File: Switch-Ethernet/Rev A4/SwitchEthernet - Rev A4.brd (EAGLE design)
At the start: 86 x 90 mm, 110 parts, among them J1 22-05-7028-02, J2 DF17(2.0)-20DP-0.5V(57), J3 DF17(4.0)-20DP-0.5V(57), J4 22-05-7058-05, P1 RB1-125BAG1A, T1 H1102FNL, T2 H1102FNL, U1 TC1264-3.3, U2 TC1264-1.8, U3 KSZ8995MA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

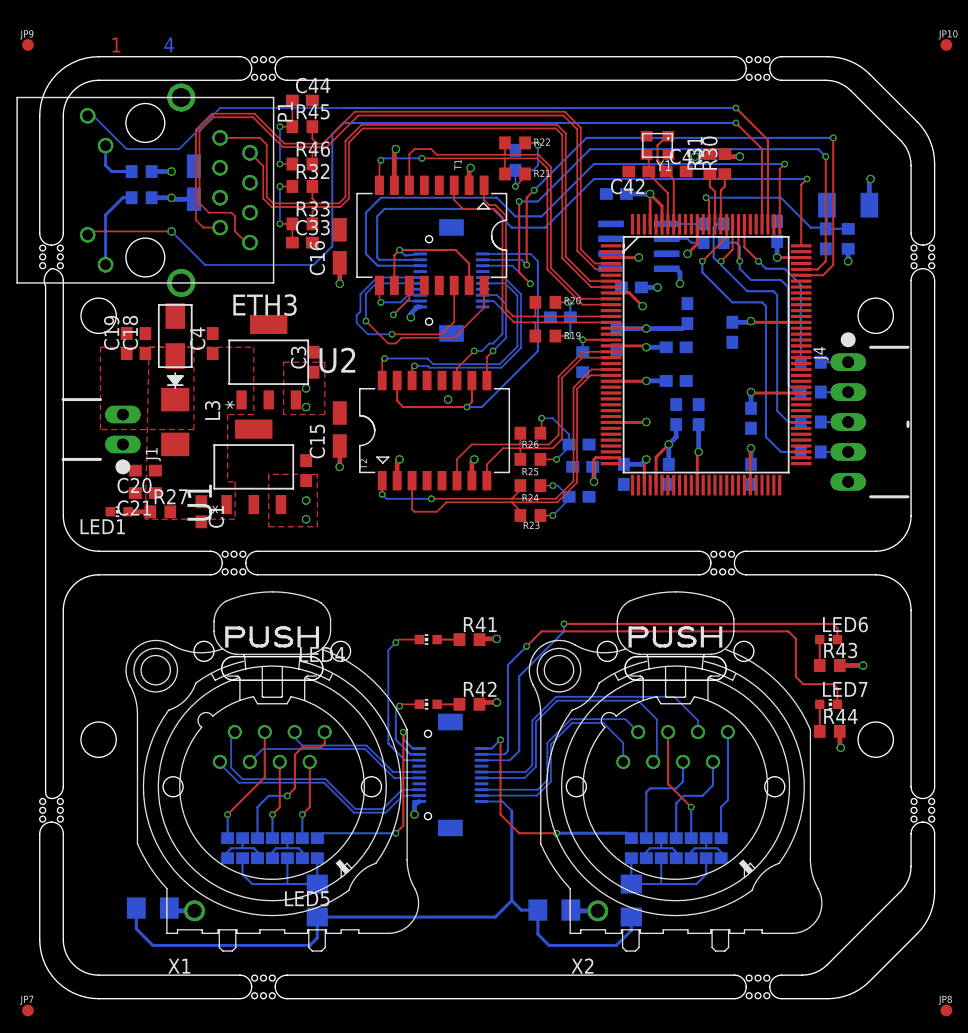
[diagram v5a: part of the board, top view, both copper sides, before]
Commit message: Add via to the guard ring
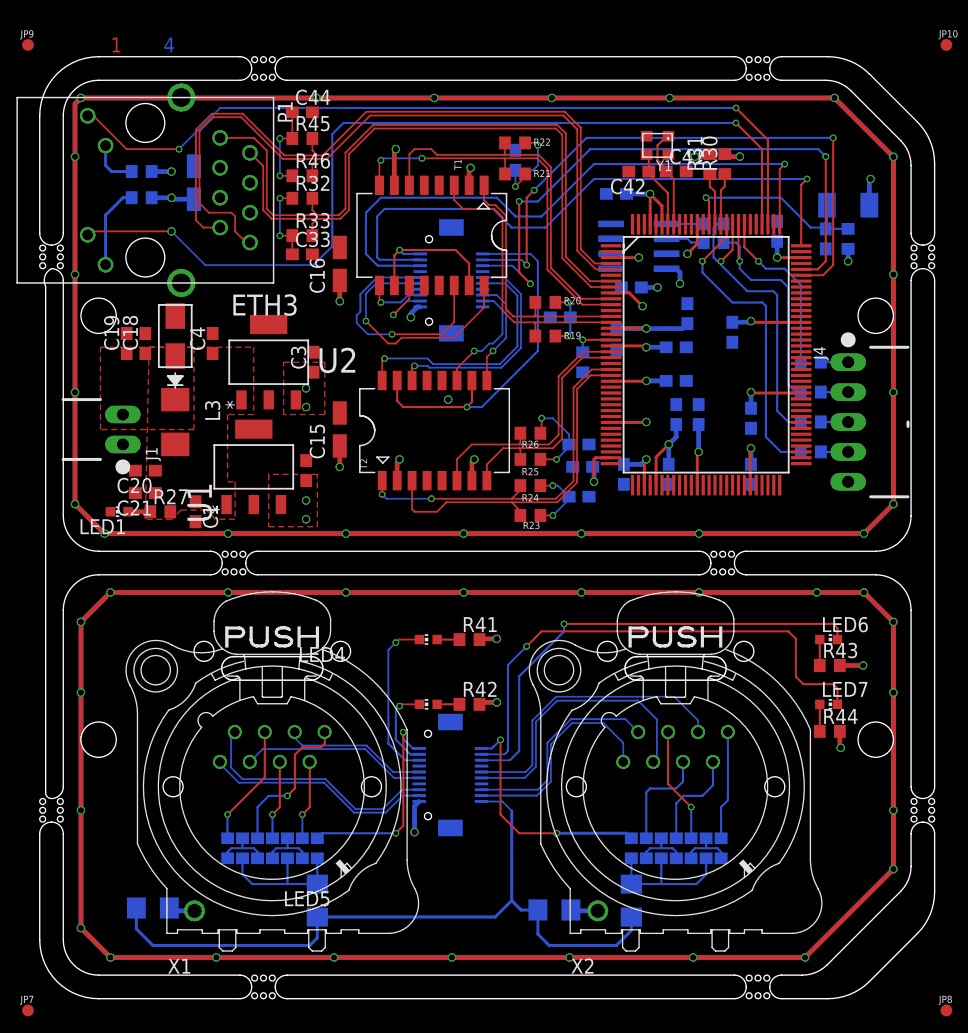
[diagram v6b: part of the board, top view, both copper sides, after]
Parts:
- moved C16 1.50 mm to (30.5, 67.4)
- moved C33 1.00 mm to (27.3, 68.2)
- moved C44 1.00 mm to (27.3, 80.3)
- moved R32 1.00 mm to (27.3, 73.0)
- moved R33 1.00 mm to (27.3, 69.8)
- moved R45 1.00 mm to (27.3, 78.1)
- moved R46 1.00 mm to (27.3, 74.9)
- moved C1 0.50 mm to (18.2, 46.4)
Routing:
- net N$2: track 0.00 -> 413.7 mm, vias 0 -> 21
- net N$1: track 0.00 -> 382.4 mm, vias 0 -> 23
- net +3V3: track 67.0 -> 68.4 mm
- net TX3_ISO_N: track 53.1 -> 54.5 mm
- net TX3_ISO_P: track 56.9 -> 58.0 mm
- net RX3_ISO_P: track 61.0 -> 61.8 mm
- net RX3_ISO_N: track 63.2 -> 64.0 mm
- net L3-2: vias 1 -> 2

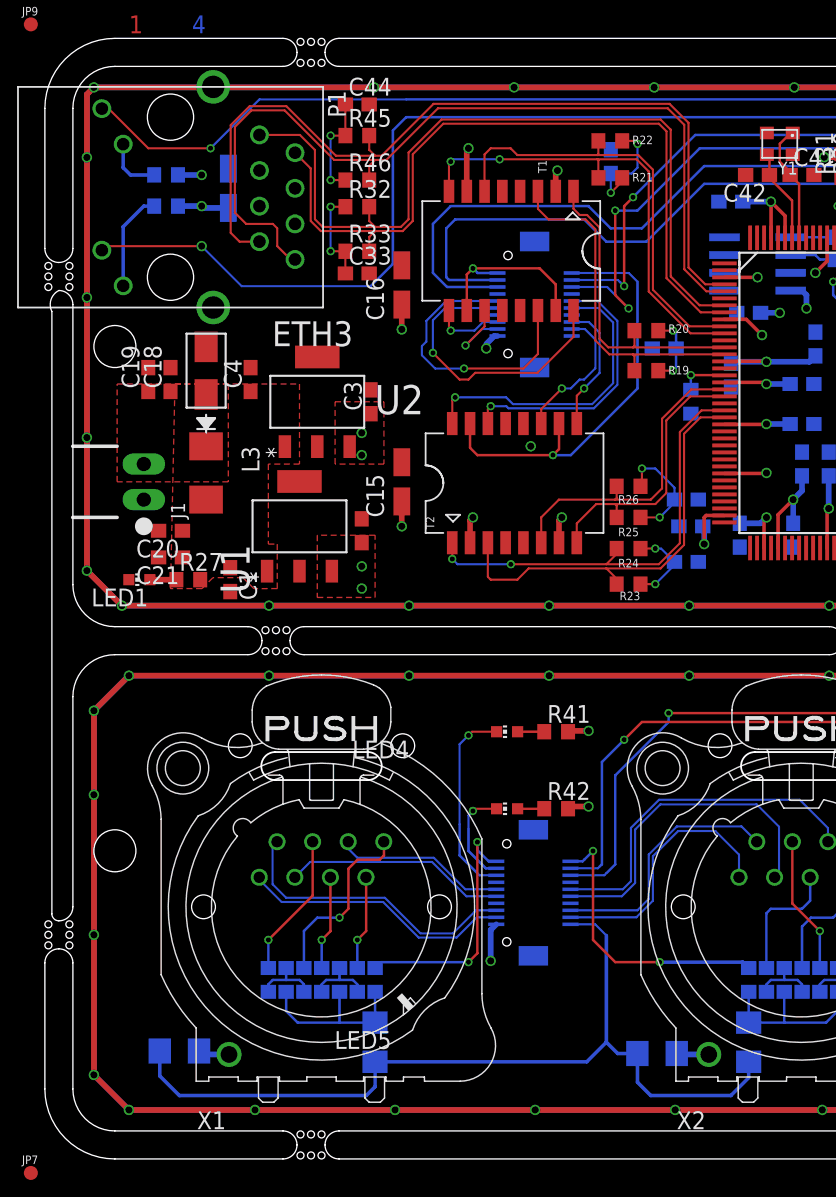
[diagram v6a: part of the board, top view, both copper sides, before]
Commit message: Connect GND meca of the connectors to the guard ring
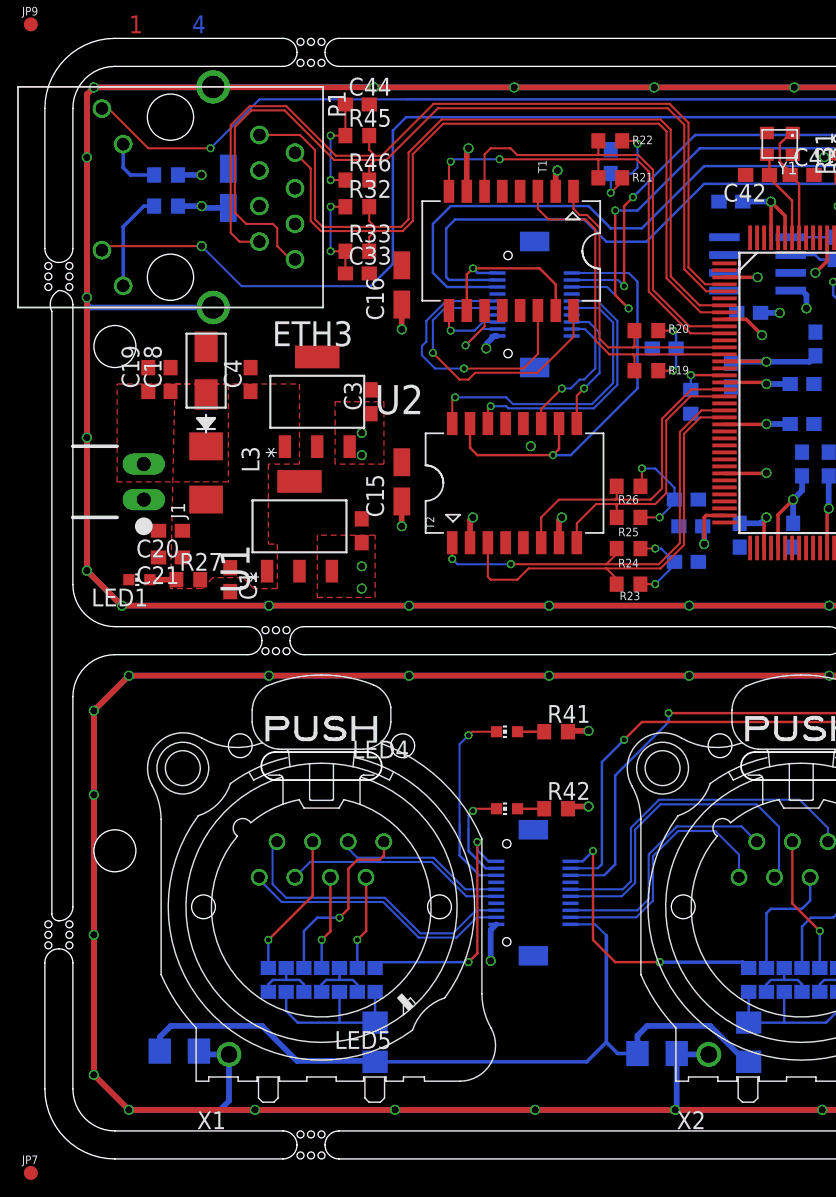
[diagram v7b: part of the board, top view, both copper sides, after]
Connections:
- removed net N$36: C47.1, X2.G
- removed net N$37: C46.1, X1.G
- new net AGND: C46.1, C47.1, P1.S1, P1.S2, X1.G, X2.G
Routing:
- net AGND: track 0.00 -> 818.1 mm, vias 0 -> 44
- net N$2: track 413.7 -> 0.00 mm, vias 21 -> 0
- net N$1: track 382.4 -> 0.00 mm, vias 23 -> 0
- net GND: track 62.0 -> 58.5 mm
- net N$36: track 2.32 -> 0.00 mm
- net N$37: track 2.24 -> 0.00 mm

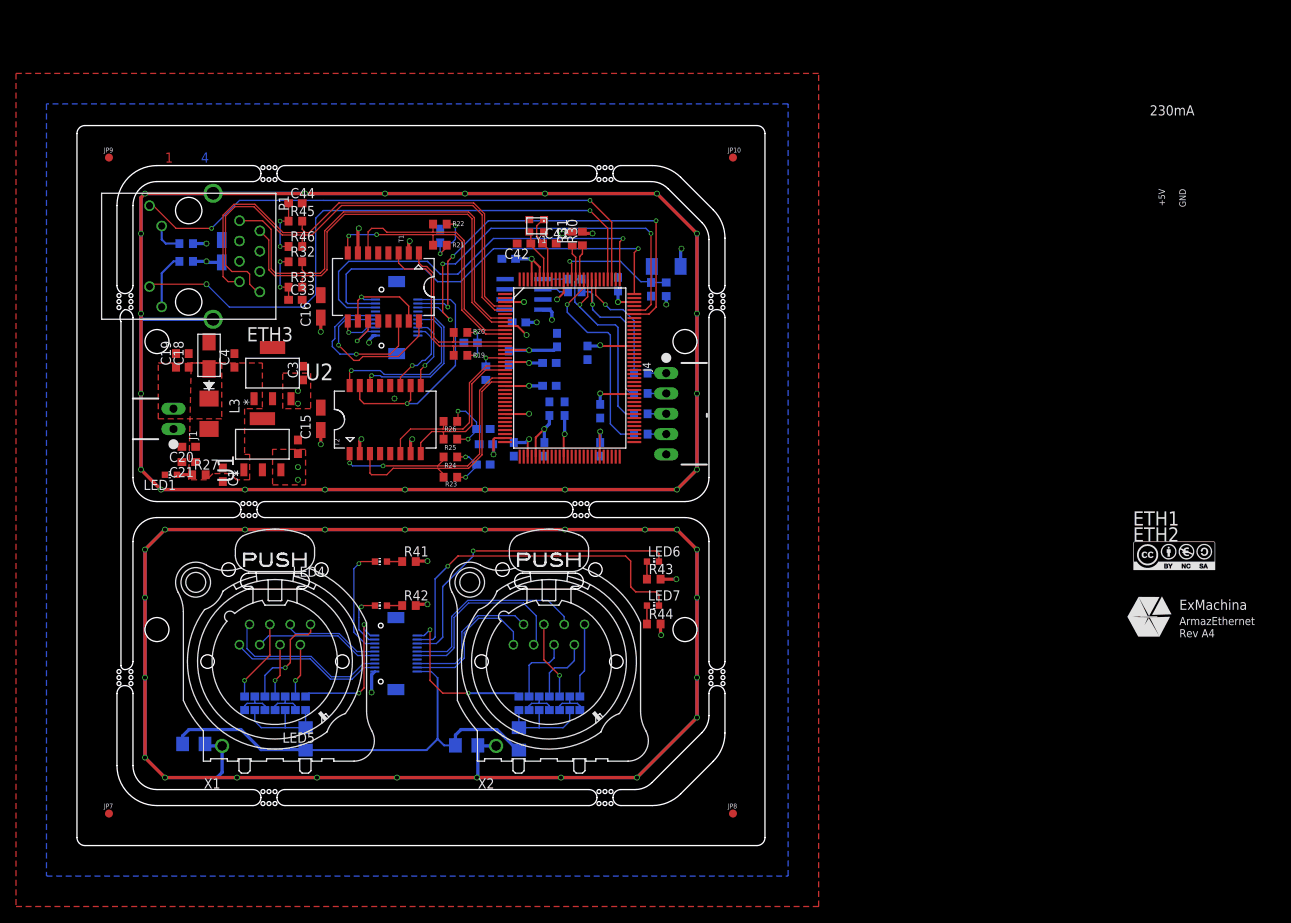
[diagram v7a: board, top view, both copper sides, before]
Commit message: Add the cotation, the board name, the logo and the CC
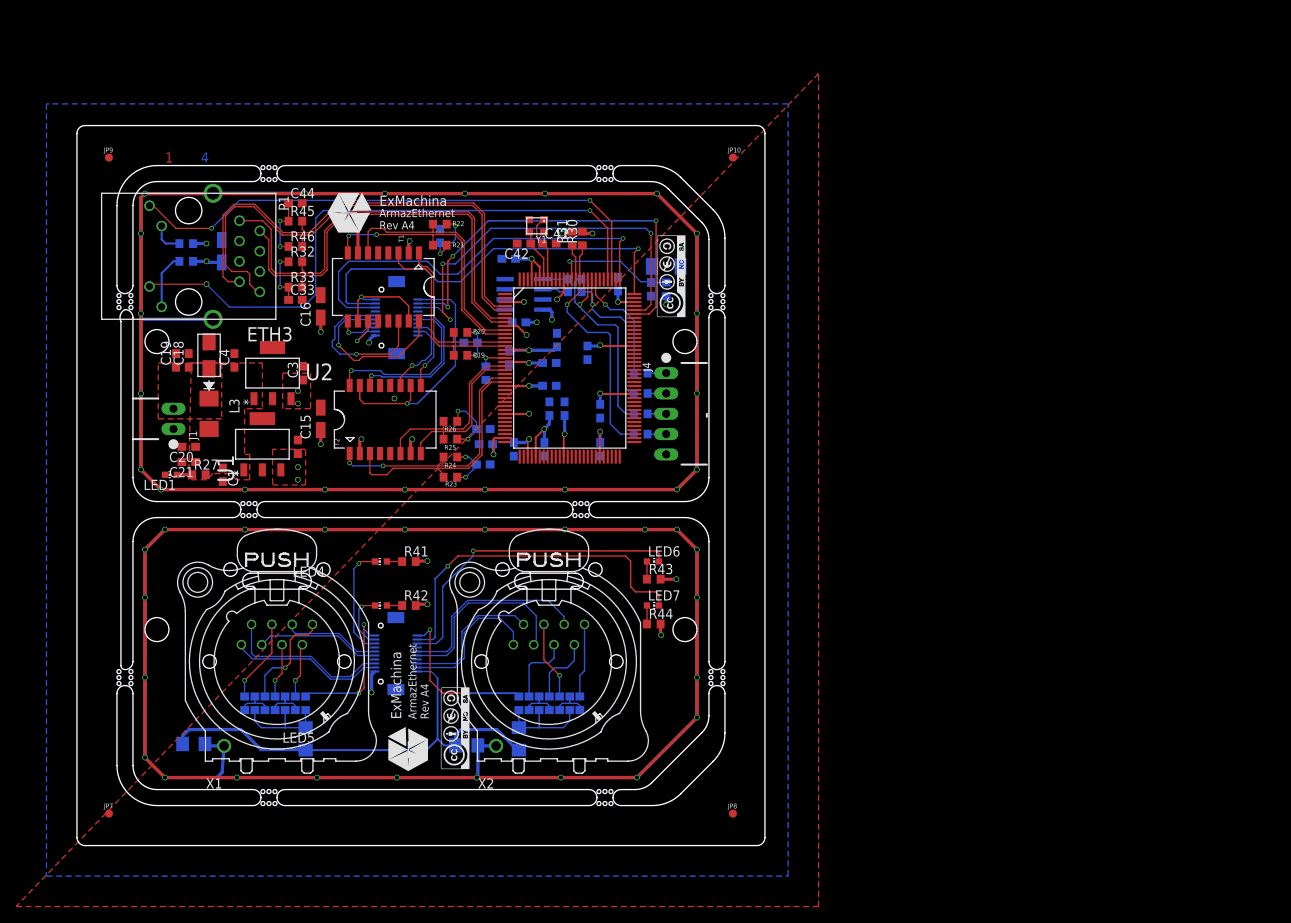
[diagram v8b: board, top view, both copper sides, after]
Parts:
- removed U$7: CC-BY-NC-SA, cc-by-sa:CC-BY-NC-SA
- added U$2, U$3: CC-BY-NC-SA, cc-by-sa:CC-BY-NC-SA
- added U$4: EXMACHINA-LOGO-NAME, exmachina:EXM-LOGO-BASELINE
- moved U$8 94.0 mm to (41.4, 12.0), turned to 90 degrees
- moved X1 0.25 mm to (25.0, 23.0)
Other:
- board text removed: "230mA"
- board text removed: "ETH1"
- board text removed: "ETH2"
- board text removed: "GND"
